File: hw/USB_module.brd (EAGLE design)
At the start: 25 x 45 mm, 34 parts, among them J1 GROVE-4P-2.0-3470130P1, J2 GROVE-4P-2.0-3470130P1, X1 22-23-2021, X2 47589-0001, X3 22-23-2021, X4 53047-04, X5 53047-04, X6 53047-06, X7 53047-06, X8 53047-06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

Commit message: work in progress
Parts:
- U$6: value STM32F103CXTX -> STM32F303C
- moved X4 58.0 mm to (76.2, 28.5)
- moved X5 58.0 mm to (76.2, 24.5)
- moved X6 58.0 mm to (67.5, 32.5)
- moved X7 58.0 mm to (67.5, 28.5)
- moved X8 58.0 mm to (67.5, 24.5)
- moved X1 26.2 mm to (37.6, 28.2)
- moved X3 17.0 mm to (36.9, 36.7)
- moved R11 15.1 mm to (8.50, 50.7)
- moved R14 15.1 mm to (7.10, 50.7)
- moved X2 15.1 mm to (7.50, 57.0)
- moved X9 8.80 mm to (22.6, 25.0), turned to 90 degrees
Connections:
- removed net N$5: X7.5, X7.6
- removed net N$6: X8.5, X8.6
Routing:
- net +3V3: track 86.4 -> 87.1 mm

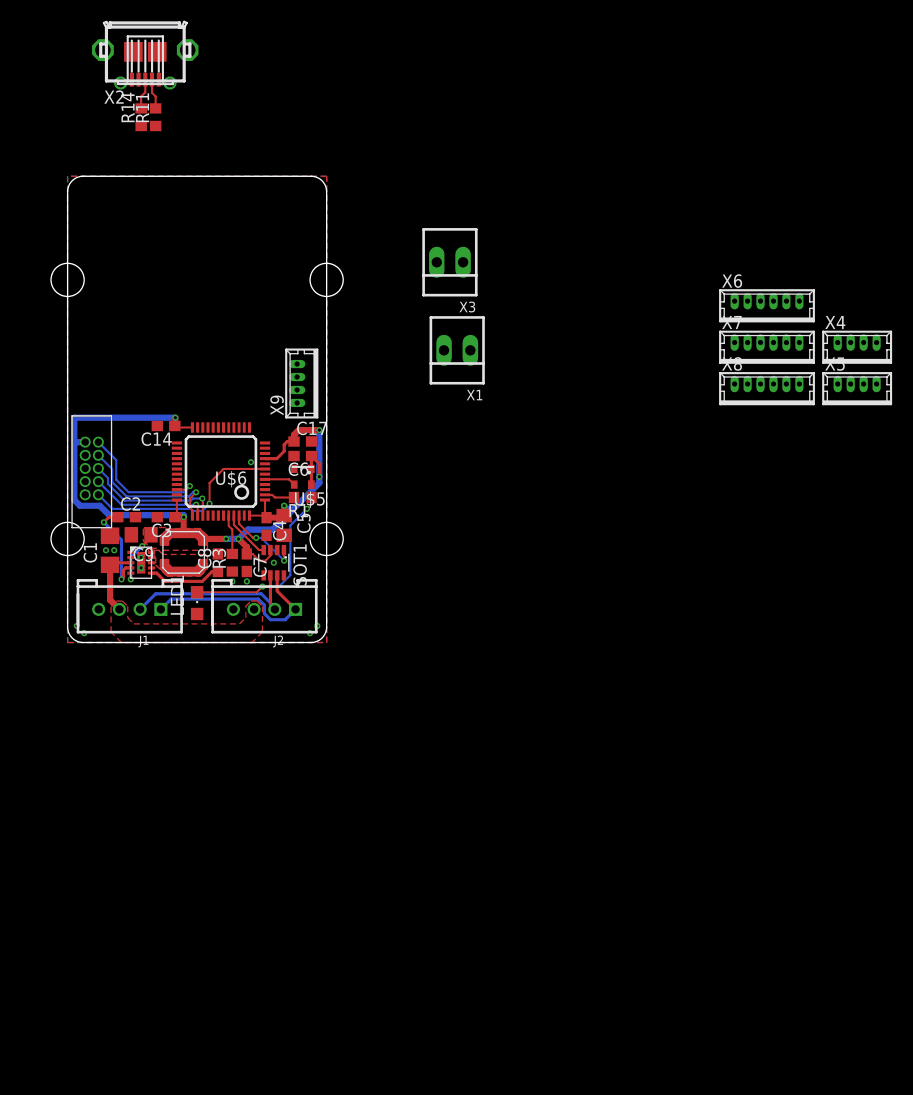
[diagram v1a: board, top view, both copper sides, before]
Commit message: layout of power oring section ongoing
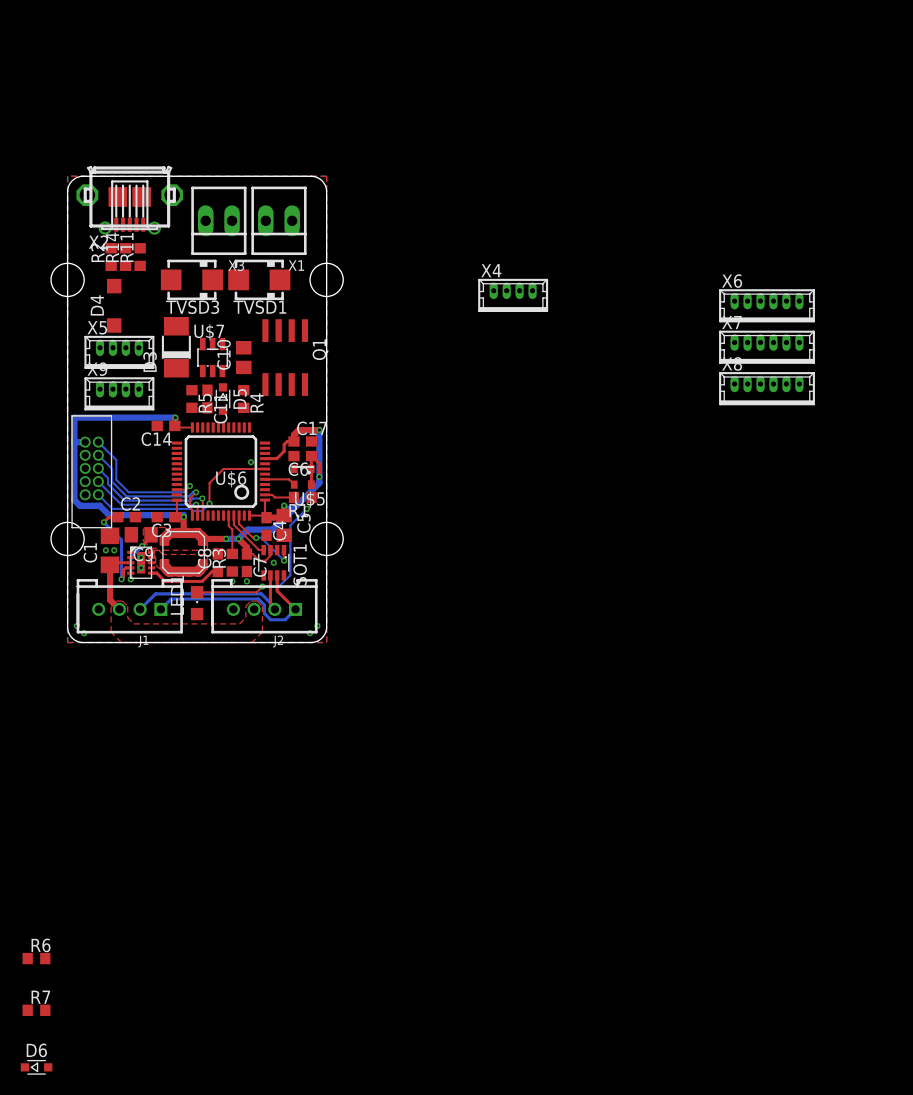
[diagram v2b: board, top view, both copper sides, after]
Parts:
- added C10: (no value), rcl:C0805
- added C11: 10nF, rcl:C0603
- added D3: (no value), diode:DO-214AC
- added D4: (no value), diode:SOD123
- added D5, D6: (no value), dp_devices:SOD-323F
- added Q1: (no value), transistor-power:SO-08
- added R2: 100k, rcl:R0603
- added R4: 4k7, rcl:R0603
- added R5: (no value), rcl:R0603
- added R6: 10k, rcl:R0603
- added R7: 1k, rcl:R0603
- added TVSD1, TVSD3: SMAJ24A, TVSD:SMA
- added U$7: LM5050-1, texas-instruments:SOT23-6L
- moved X5 71.3 mm to (5.00, 28.0)
- moved X4 33.6 mm to (43.0, 33.5)
- moved X3 22.7 mm to (14.6, 40.7)
- moved X1 21.3 mm to (20.4, 40.7)
- moved X9 17.6 mm to (5.00, 24.0), turned to 0 degrees
- moved X2 14.1 mm to (6.00, 43.0)
- moved R11 13.6 mm to (7.00, 37.2)
- moved R14 13.6 mm to (5.60, 37.2)
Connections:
- removed net USB_ID: X2.4
- new net N$10: C11.1, R5.1, U$7.1
- new net N$5: R2.2, X2.4
- new net N$6: D5.C, R4.1, U$7.3
- new net N$9: Q1.4, U$7.5
- new net VBATT: C10.2, Q1.1, Q1.2, Q1.3, R6.2, TVSD1.C, U$7.4, X1.1
- new net VPSU: D3.A, R4.2, TVSD3.C, X3.1
- new net VSENSE: D6.C, R6.1, R7.2
- net GND: now also C10.1, C11.2, D5.A, D6.A, R2.1, R7.1, TVSD1.A, TVSD3.A, U$7.2, X1.2, X3.2
- net USB_VBUS: now also D4.A
- net VIN: now also D3.C, D4.C, Q1.5, Q1.6, Q1.7, Q1.8, R5.2, U$7.6
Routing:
- net N$32: track 2.94 -> 0.00 mm
- net N$3: track 2.91 -> 0.00 mm

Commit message: layout almost finished
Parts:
- removed D3: (no value), diode:DO-214AC
- removed D4: (no value), diode:SOD123
- removed D5: (no value), dp_devices:SOD-323F
- removed TVSD3: SMAJ24A, TVSD:SMA
- removed X3: 22-23-2021, con-molex:22-23-2021
- removed X7, X8: 53047-06, con-molex:53047-06
- removed X9: 53047-04, con-molex:53047-04
- added C12: (no value), rcl:E3,5-8
- added D1: MBR0520LT, diode:SOD123
- added D2: (no value), dp_devices:SOD-323F
- added R8: 22, rcl:R0603
- D6: value (none) -> 3V
- moved D6 68.4 mm to (14.1, 25.2)
- moved X6 65.2 mm to (2.50, 27.0), turned to 90 degrees
- moved R7 64.6 mm to (14.0, 26.8), turned to 180 degrees
- moved R6 61.1 mm to (14.0, 28.2)
- moved X4 37.3 mm to (6.50, 25.8), turned to 90 degrees
- moved R4 14.8 mm to (9.40, 36.2), turned to 90 degrees
- moved C11 7.52 mm to (14.0, 31.0), turned to 0 degrees
- moved C10 7.25 mm to (15.1, 34.5)
- moved U$7 7.16 mm to (12.1, 34.4)
- moved R5 6.42 mm to (14.0, 29.6), turned to 0 degrees
- moved TVSD1 6.26 mm to (15.5, 40.5), turned to 270 degrees
- moved Q1 6.04 mm to (19.0, 33.2)
- moved X5 5.92 mm to (10.5, 25.8), turned to 90 degrees
- moved R11 1.41 mm to (8.00, 36.2)
- moved R14 1.41 mm to (6.60, 36.2)
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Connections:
- removed net USB_DM: R11.1
- removed net USB_DP: R14.1
- removed net VPSU: D3.A, R4.2, TVSD3.C, X3.1
- new net !CS: U$6.25, X6.3
- new net MISO: U$6.27, X6.5
- new net MOSI: U$6.28, X6.6
- new net SCK: U$6.26, X6.4
- new net SCL: U$6.30, X4.3
- new net SDA: U$6.31, X4.4
- new net UART_RX: U$6.22, X5.4
- new net UART_TX: U$6.21, X5.3
- new net USB_N: R11.1, U$6.32
- new net USB_P: R14.1, U$6.33
- net +3V3: now also R8.1, X4.1, X5.1, X6.1
- net GND: now also C12.-, D2.A, X4.2, X5.2, X6.2; no longer D5.A, TVSD3.A, X3.2
- net N$32: now also R8.2
- net N$6: now also D2.C; no longer D5.C
- net USB_VBUS: now also D1.A, R4.2; no longer D4.A
- net VBATT: no longer R6.2
- net VIN: now also C12.+, D1.C, R6.2; no longer D3.C, D4.C
- net VSENSE: now also U$6.20
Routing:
- net USB_P: track 0.00 -> 24.8 mm
- net USB_N: track 0.00 -> 24.5 mm
- net VIN: track 7.26 -> 30.7 mm, vias 0 -> 2
- net +3V3: track 87.1 -> 107.2 mm, vias 9 -> 10
- net !CS: track 0.00 -> 14.4 mm, vias 0 -> 1
- net SCK: track 0.00 -> 13.7 mm, vias 0 -> 1
- net MISO: track 0.00 -> 12.7 mm, vias 0 -> 1
- net MOSI: track 0.00 -> 11.9 mm, vias 0 -> 1
- net SCL: track 0.00 -> 11.4 mm
- net USB_VBUS: track 0.00 -> 10.7 mm
- net SDA: track 0.00 -> 10.3 mm
- net VSENSE: track 0.00 -> 7.97 mm
- net N$9: track 0.00 -> 6.94 mm
- net N$6: track 0.00 -> 6.60 mm, vias 0 -> 2
- net UART_TX: track 0.00 -> 6.09 mm
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- added copper zone on layer 1, net VBATT

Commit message: layout completed
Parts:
- moved U$5 0.51 mm to (22.6, 16.5)
- moved C10 0.50 mm to (15.1, 34.0)
- moved C17 0.50 mm to (22.7, 19.9)
- moved C6 0.50 mm to (22.7, 18.5)
- moved D1 0.30 mm to (12.2, 40.5)
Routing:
- net VIN: track 30.7 -> 66.4 mm
- net N$4: track 14.5 -> 34.2 mm
- net +3V3: track 107.2 -> 114.5 mm
- net CAN_TX: track 7.66 -> 11.3 mm
- net VBATT: track 5.76 -> 7.29 mm
- net N$9: track 6.94 -> 6.19 mm
